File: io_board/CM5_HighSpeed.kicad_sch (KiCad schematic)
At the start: 10 parts, among them J16 Conn_01x22_Female, J5 Conn_01x22_Female, U6 AP22653W6

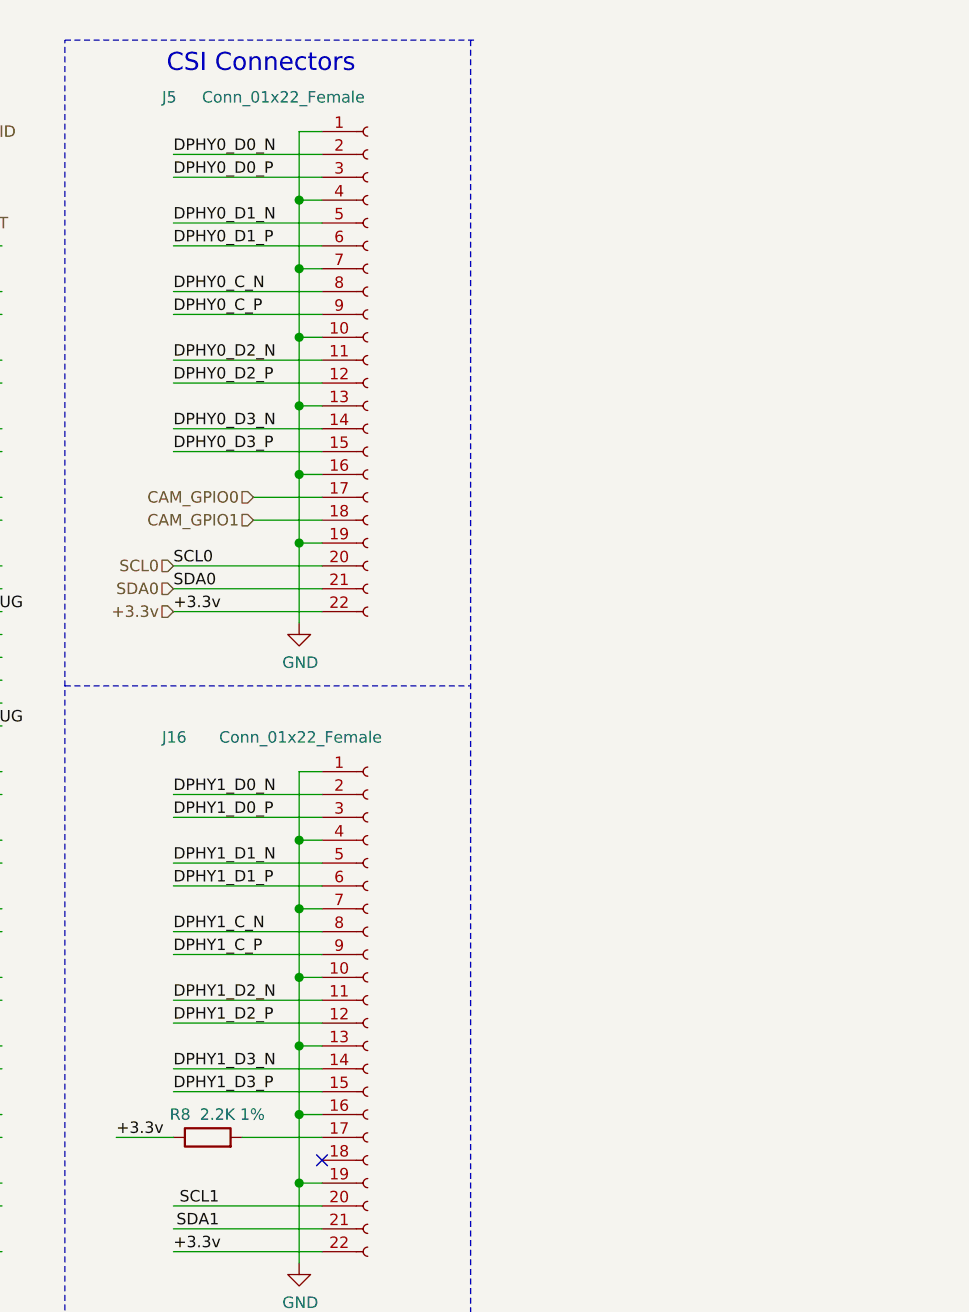
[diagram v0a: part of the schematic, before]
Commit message: Added necessary extra connetors and swapped camera to vertical.
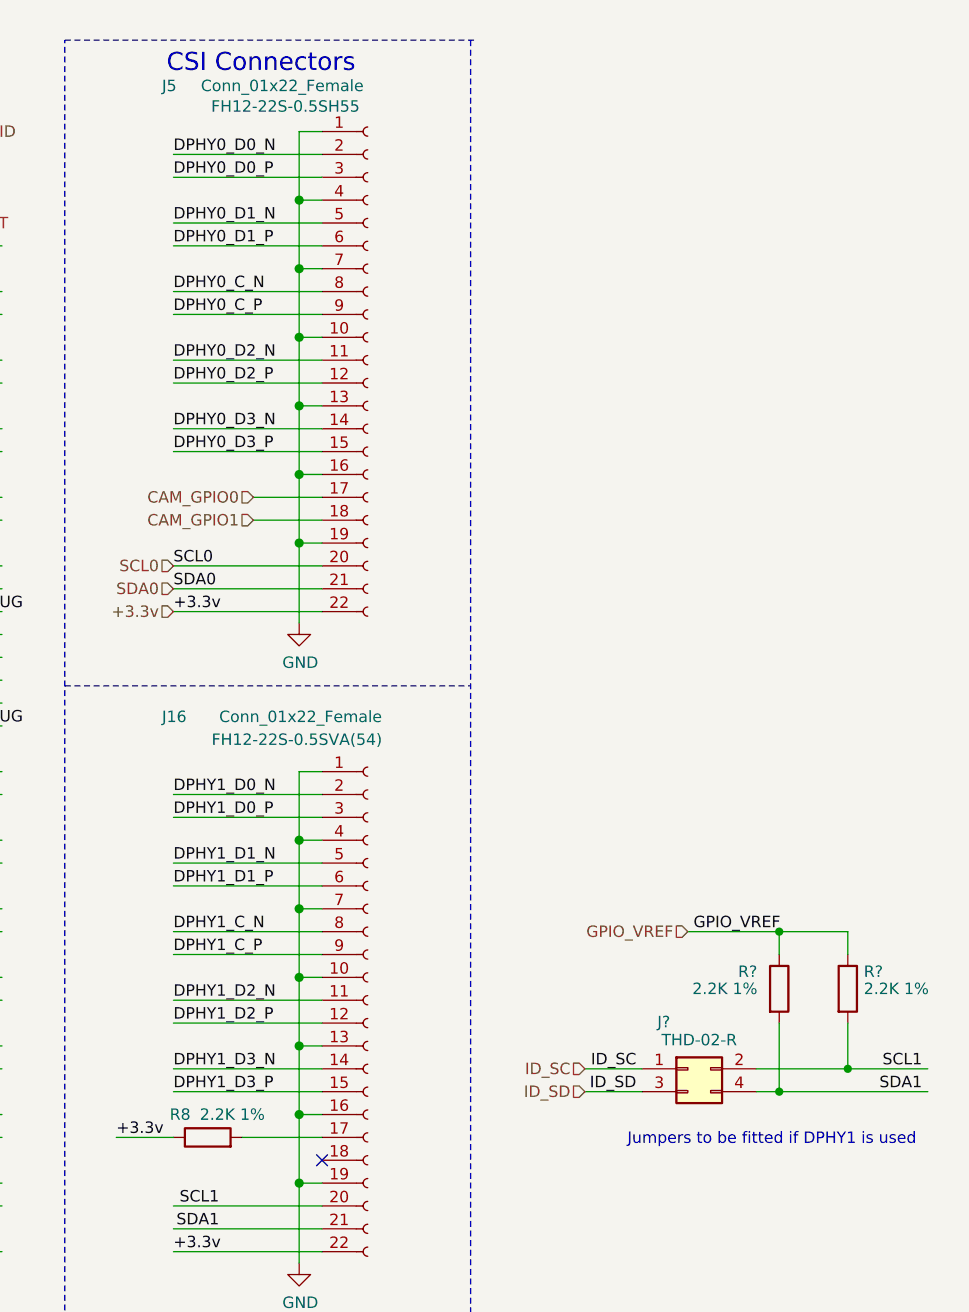
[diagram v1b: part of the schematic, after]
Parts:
- added J?: THD-02-R, Connector_PinHeader_2.54mm:PinHeader_2x02_P2.54mm_Vertical, symbol Connector_Generic:Conn_02x02_Odd_Even
- added R? (x2): 2.2K 1%, Resistor_SMD:R_0402_1005Metric, symbol Device:R
- J16: footprint CM5IO:Hirose_FH12-22S-0.5SH_1x22-1MP_P0.50mm_Horizontal -> FH12-22S-0.5SVA_54_:FH1222S05SVA54; Field5 798-FH12-22S-0.5SH55 -> 798-FH1222S0.5SVA54; Field6 FH12-22S-0.5SH55 -> FH12-22S-0.5SVA(54); Part Description 22 Position FFC, FPC Connector Contacts, Bottom 0.020" (0.5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 -> FFC & FPC Connectors 0.5MM 22P SMT VERT MNT SELECT GLD
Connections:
- net SCL1: now also J?.2 (Pin_2), R?.2
- net SDA1: now also J?.4 (Pin_4), R?.2
- new net GPIO_VREF: R?.1, R?.1
- new net ID_SC: J?.1 (Pin_1)
- new net ID_SD: J?.3 (Pin_3)
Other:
- note added: "Jumpers to be fitted if DPHY1 is used"

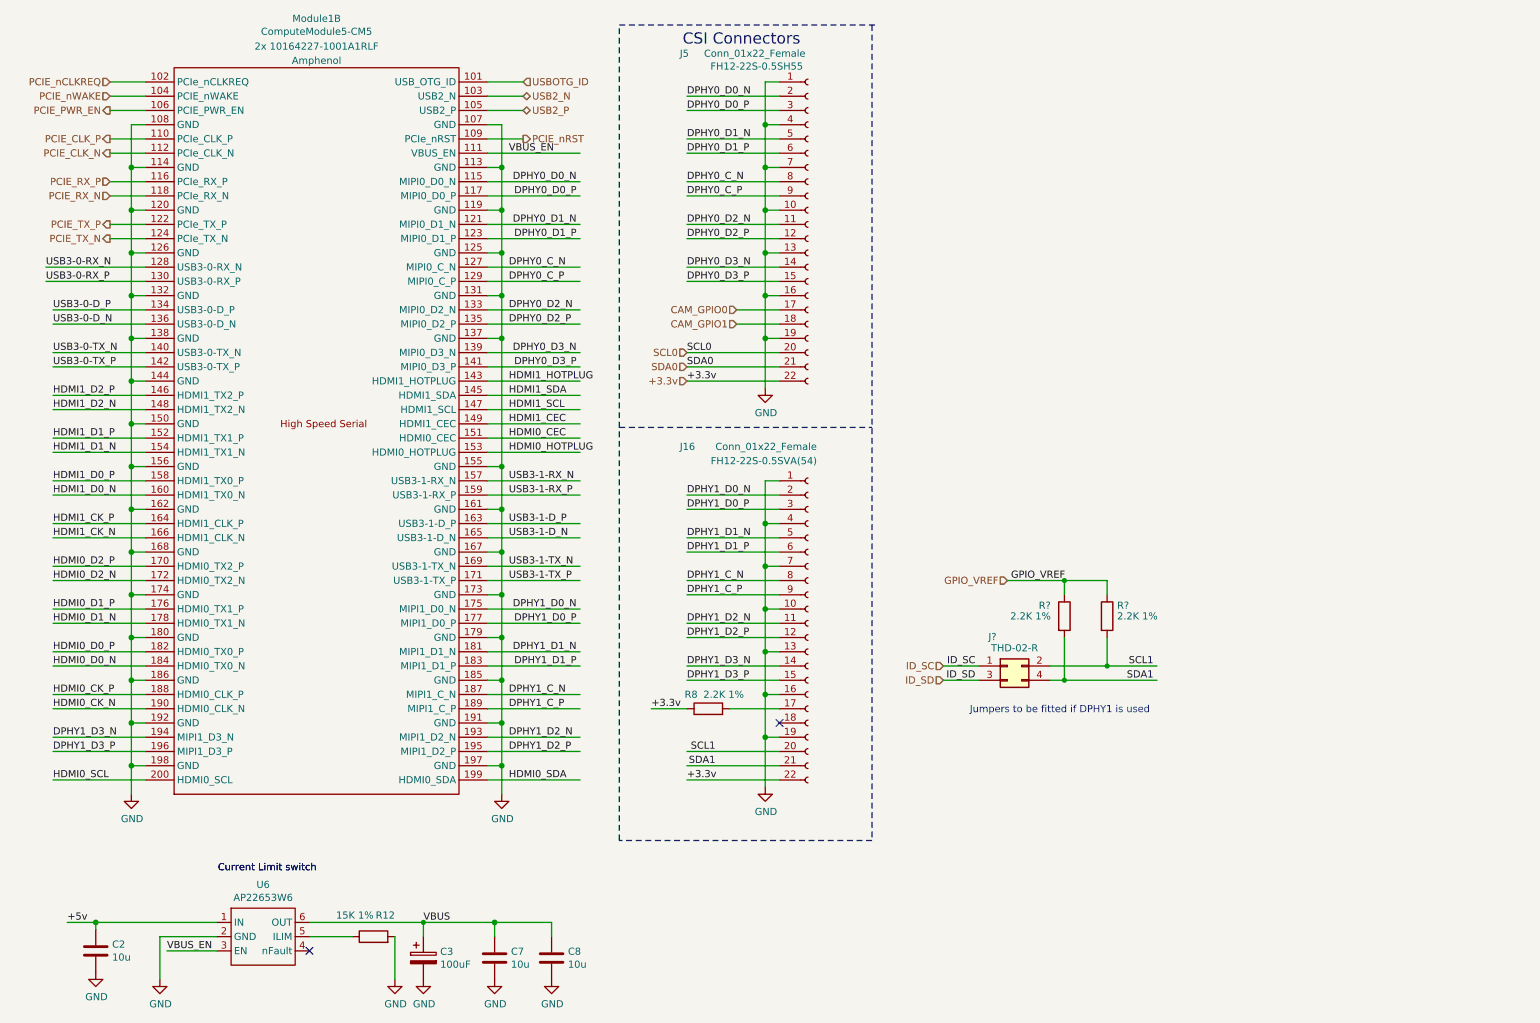
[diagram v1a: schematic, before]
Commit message: Assigned pins to I2C, UART, PWM, SPI ports.
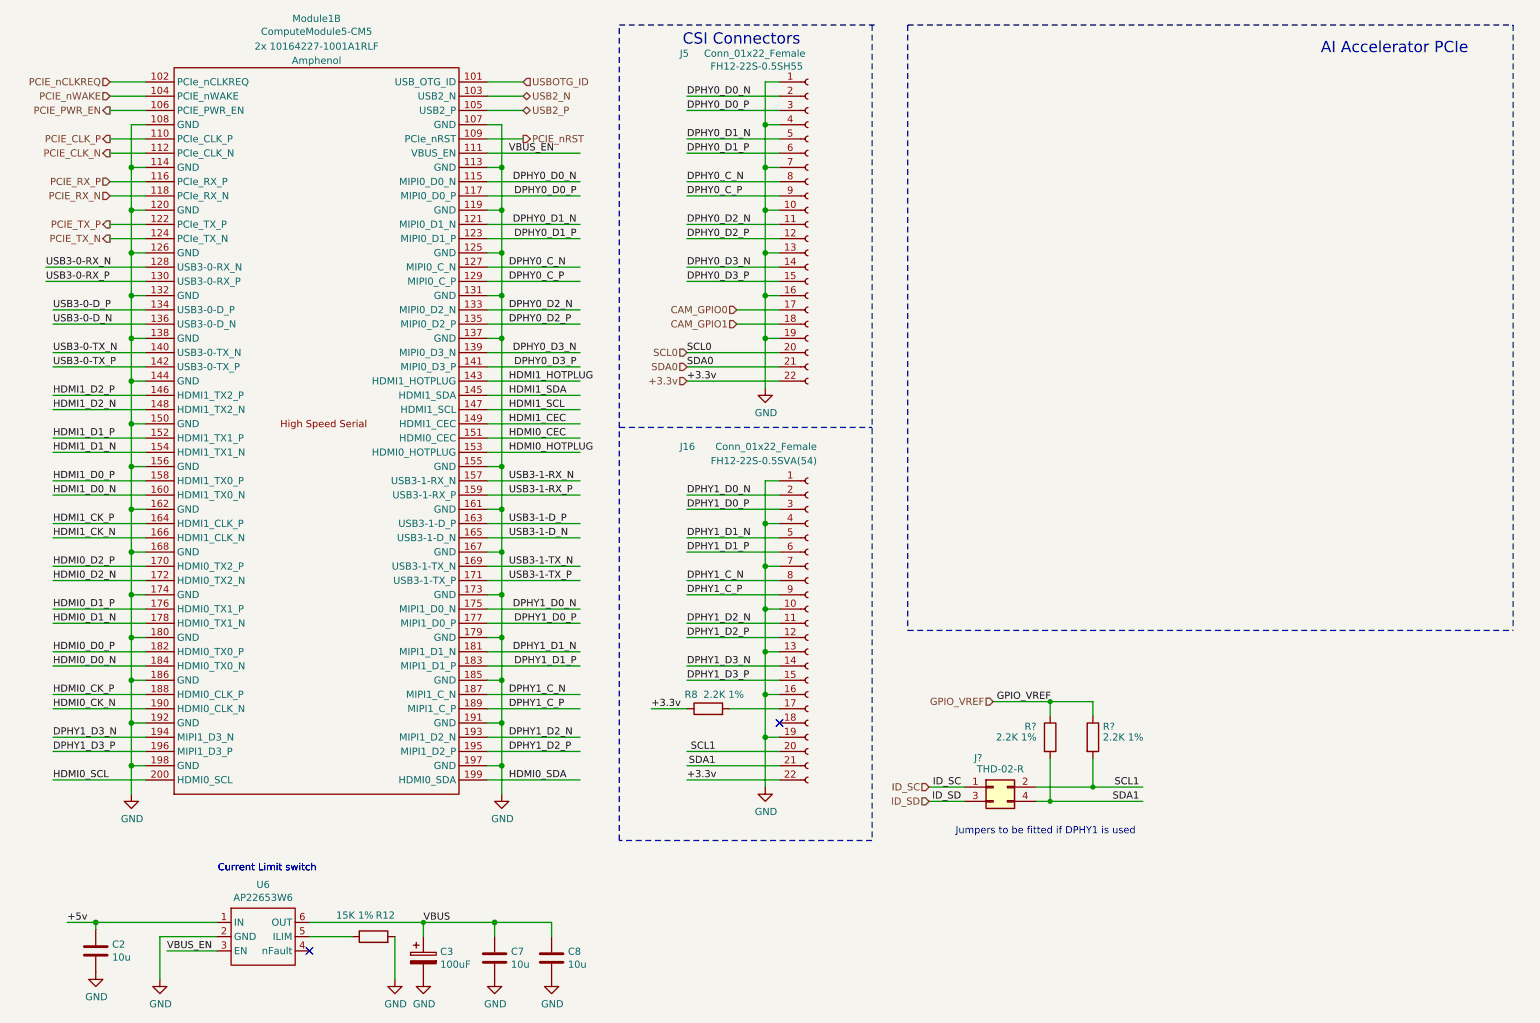
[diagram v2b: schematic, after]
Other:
- note added: "AI Accelerator PCIe"
- moved on the sheet: J?, R?

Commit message: Connected USB 3.0 and added part number for PCIe.
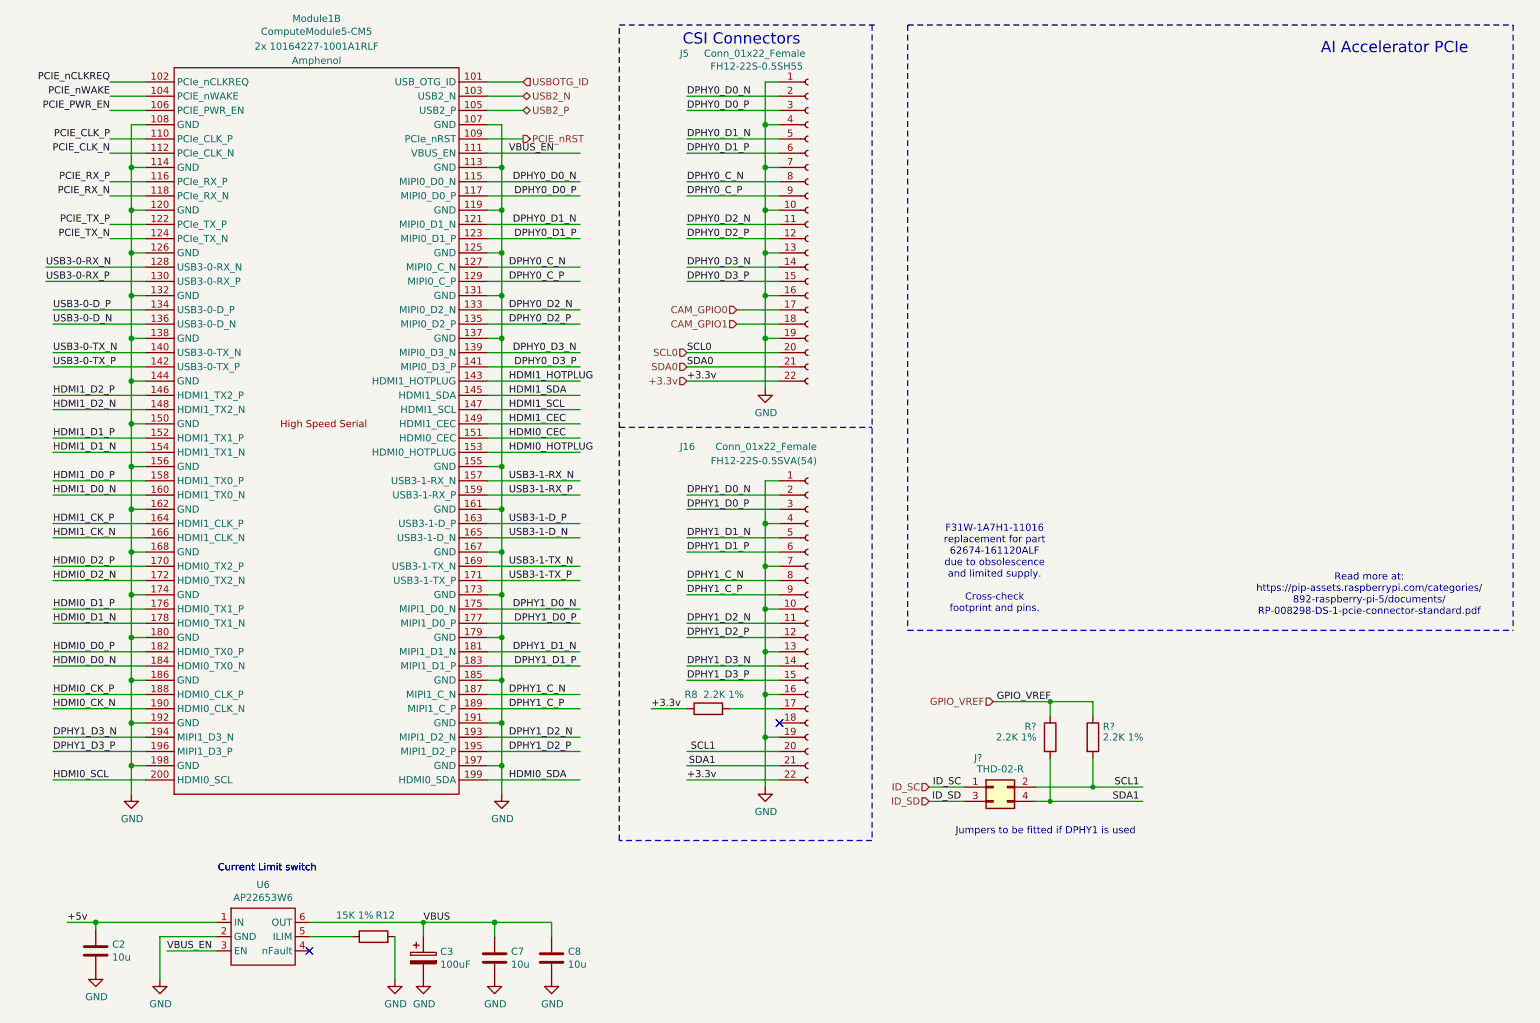
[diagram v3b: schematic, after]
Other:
- note added: "F31W-1A7H1-11016 replacement for part 62674-161120ALF due to obsolescence and limited supply. Cross-check footprint and pins."
- note added: "Read more at: https://pip-assets.raspberrypi.com/categories/ 892-raspberry-pi-5/documents/ RP-008298-DS-1-pcie-connector-standard.pdf"
- company: Copyright © 2024 Raspberry Pi Ltd. -> Copyright © 2024 Raspberry Pi Ltd. & Ilias Kringos
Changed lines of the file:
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@@
 		(title "Compute Module 5 IO Board - CM5 - Highspeed")
 		(rev "1")
-		(company "Copyright © 2024 Raspberry Pi Ltd.")
+		(company "Copyright © 2024 Raspberry Pi Ltd. & Ilias Kringos")
 		(comment 1 "www.raspberrypi.com")
 	)
+	(text "Read more at:\nhttps://pip-assets.raspberrypi.com/categories/\n892-raspberry-pi-5/documents/\nRP-008298-DS-1-pcie-connector-standard.pdf"
+		(exclude_from_sim no)
+		(at 256.286 120.65 0)
+		(effects
+			(font
+				(size 1.27 1.27)
+			)
+			(justify bottom)
+		)
+	)
+	(text "F31W-1A7H1-11016 \nreplacement for part\n62674-161120ALF\ndue to obsolescence \nand limited supply.\n\nCross-check\nfootprint and pins."
+		(exclude_from_sim no)
+		(at 189.484 120.142 0)
+		(effects
+			(font
+				(size 1.27 1.27)
+			)
+			(justify bottom)
+		)
+	)
 	(text "Current Limit switch"
 		(exclude_from_sim no)
@@
 		)
 	)
+	(label "PCIE_nWAKE"
+		(at 31.75 27.94 180)
+		(effects
+			(font
+				(size 1.27 1.27)
+			)
+			(justify right bottom)
+		)
+	)
 	(label "DPHY0_D2_N"
 		(at 134.62 50.8 0)
@@
 		)
 	)
+	(label "PCIE_RX_P"
+		(at 31.75 43.18 180)
+		(effects
+			(font
+				(size 1.27 1.27)
+			)
+			(justify right bottom)
+		)
+	)
 	(label "USB3-1-D_N"
 		(at 102.87 106.68 0)
@@
 		)
 	)
+	(label "PCIE_CLK_N"
+		(at 31.75 38.1 180)
+		(effects
+			(font
+				(size 1.27 1.27)
+			)
+			(justify right bottom)
+		)
+	)
 	(label "DPHY1_D1_P"
 		(at 134.62 109.22 0)
@@
 		)
 	)
+	(label "PCIE_RX_N"
+		(at 31.75 45.72 180)
+		(effects
+			(font
+				(size 1.27 1.27)
+			)
+			(justify right bottom)
+		)
+	)
 	(label "HDMI0_CK_N"
 		(at 21.59 137.16 0)
@@
 		)
 	)
+	(label "PCIE_TX_N"
+		(at 31.75 53.34 180)
+		(effects
+			(font
+				(size 1.27 1.27)
+			)
+			(justify right bottom)
+		)
+	)
 	(label "DPHY1_D3_P"
 		(at 134.62 132.08 0)
@@
 		)
 	)
+	(label "PCIE_PWR_EN"
+		(at 31.75 30.48 180)
+		(effects
+			(font
+				(size 1.27 1.27)
+			)
+			(justify right bottom)
+		)
+	)
 	(label "DPHY1_D0_N"
 		(at 134.62 99.06 0)
@@
 		)
 	)
+	(label "PCIE_nCLKREQ"
+		(at 31.75 25.4 180)
+		(effects
+			(font
+				(size 1.27 1.27)
+			)
+			(justify right bottom)
+		)
+	)
 	(label "USB3-0-RX_P"
 		(at 20.32 60.96 0)
@@
 		)
 	)
+	(label "PCIE_CLK_P"
+		(at 31.75 35.56 180)
+		(effects
+			(font
+				(size 1.27 1.27)
+			)
+			(justify right bottom)
+		)
+	)
 	(label "DPHY0_C_P"
 		(at 134.62 45.72 0)
@@
 		)
 	)
+	(label "PCIE_TX_P"
+		(at 31.75 50.8 180)
+		(effects
+			(font
+				(size 1.27 1.27)
+			)
+			(justify right bottom)
+		)
+	)
 	(label "+3.3v"
 		(at 128.27 137.16 0)
@@
 		)
 	)
-	(hierarchical_label "PCIE_PWR_EN"
-		(shape output)
-		(at 31.75 30.48 180)
-		(effects
-			(font
-				(size 1.27 1.27)
-			)
-			(justify right)
-		)
-	)
-	(hierarchical_label "PCIE_CLK_P"
-		(shape output)
-		(at 31.75 35.56 180)
-		(effects
-			(font
-				(size 1.27 1.27)
-			)
-			(justify right)
-		)
-	)
 	(hierarchical_label "CAM_GPIO0"
 		(shape input)
@@
 		)
 	)
-	(hierarchical_label "PCIE_RX_N"
-		(shape input)
-		(at 31.75 45.72 180)
-		(effects
-			(font
-				(size 1.27 1.27)
-			)
-			(justify right)
-		)
-	)
 	(hierarchical_label "ID_SC"
 		(shape input)
@@
 		)
 	)
-	(hierarchical_label "PCIE_nCLKREQ"
-		(shape input)
-		(at 31.75 25.4 180)
-		(effects
-			(font
-				(size 1.27 1.27)
-			)
-			(justify right)
-		)
-	)
-	(hierarchical_label "PCIE_RX_P"
-		(shape input)
-		(at 31.75 43.18 180)
-		(effects
-			(font
-				(size 1.27 1.27)
-			)
-			(justify right)
-		)
-	)
 	(hierarchical_label "+3.3v"
 		(shape input)
@@
 		)
 	)
-	(hierarchical_label "PCIE_TX_P"
-		(shape output)
-		(at 31.75 50.8 180)
-		(effects
-			(font
-				(size 1.27 1.27)
-			)
-			(justify right)
-		)
-	)
-	(hierarchical_label "PCIE_nWAKE"
-		(shape input)
-		(at 31.75 27.94 180)
-		(effects
-			(font
-				(size 1.27 1.27)
-			)
-			(justify right)
-		)
-	)
-	(hierarchical_label "PCIE_CLK_N"
-		(shape output)
-		(at 31.75 38.1 180)
-		(effects
-			(font
-				(size 1.27 1.27)
-			)
-			(justify right)
-		)
-	)
 	(hierarchical_label "PCIE_nRST"
 		(shape output)
@@
 		(effects
 			(font
-				(size 1.27 1.27)
-			)
-			(justify right)
-		)
-	)
-	(hierarchical_label "PCIE_TX_N"
-		(shape output)
-		(at 31.75 53.34 180)
-		(effects
-			(font
